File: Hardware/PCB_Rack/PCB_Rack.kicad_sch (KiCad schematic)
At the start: 31 parts, among them J1 Conn_01x03, SW1 SW_MEC_5G, SW2 SW_Push, U1 PCF8575DBR

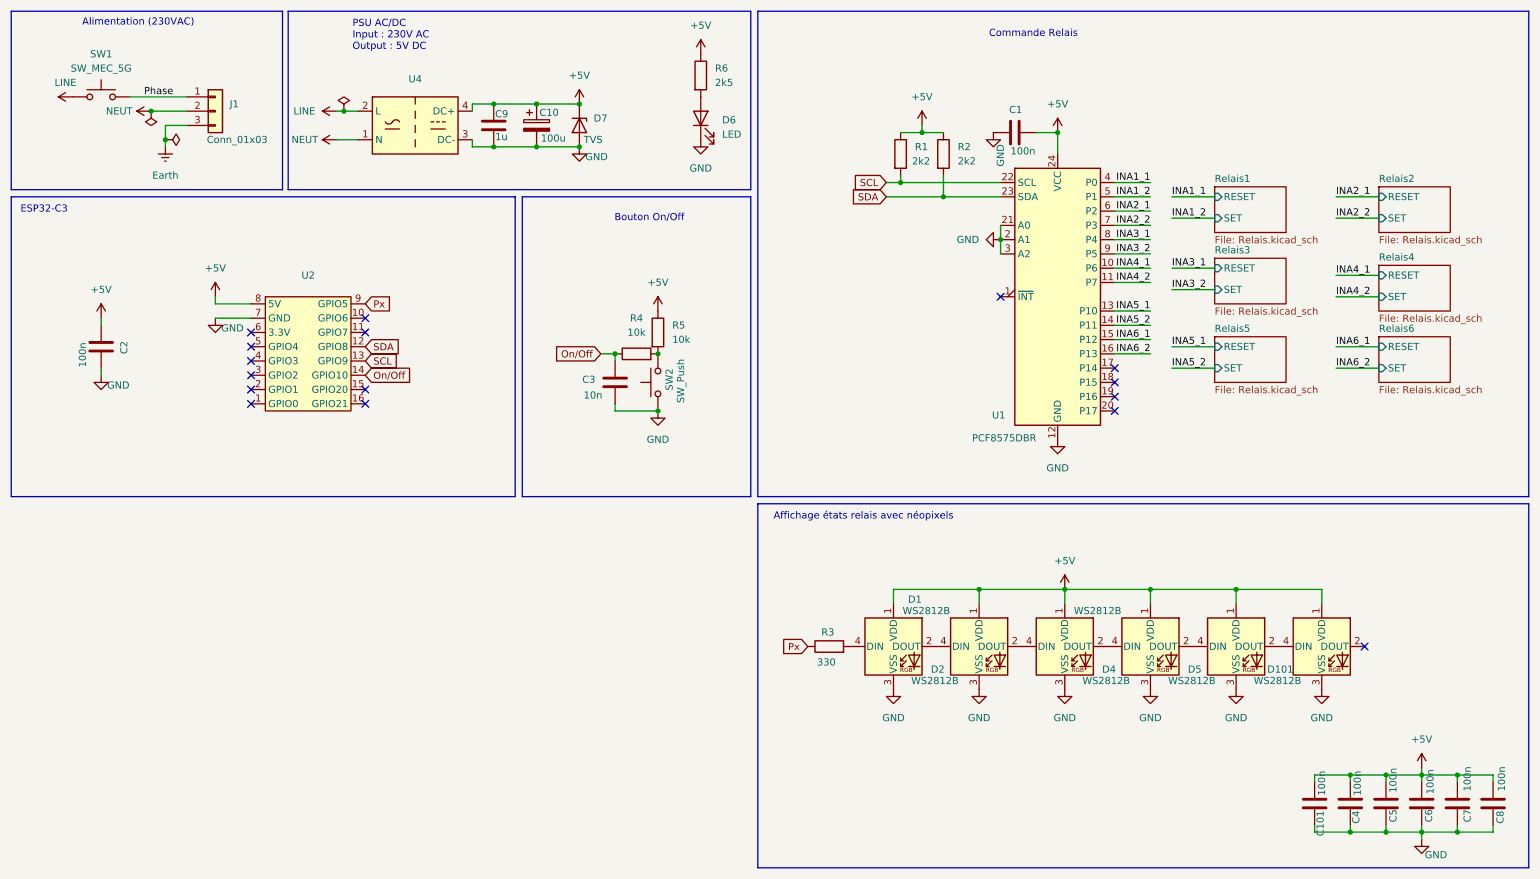
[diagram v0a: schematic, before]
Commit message: finalisation 2.0 schematic PCB RACK et début PCB
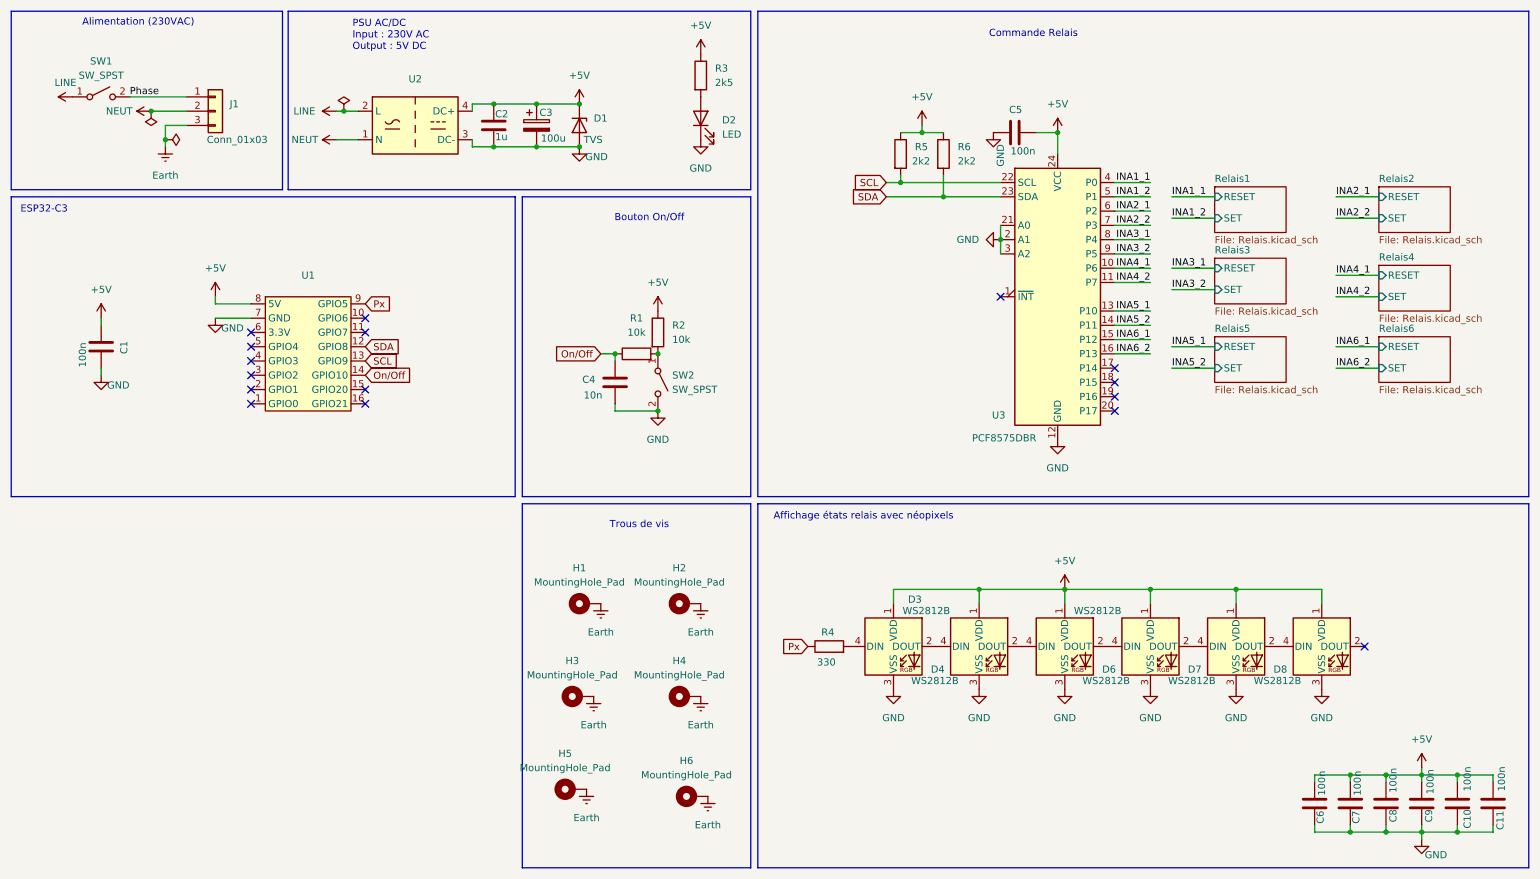
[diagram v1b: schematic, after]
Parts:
- removed SW1: SW_MEC_5G, Switch:Wurth_2pin_P5.0mm, symbol Switch:SW_MEC_5G
- removed SW2: SW_Push, Switch:Wurth_2pin_P5.0mm, symbol Switch:SW_Push
- added H1, H2, H3, H4, H5, H6: MountingHole_Pad, MountingHole:MountingHole_3.2mm_M3_DIN965_Pad_TopBottom, symbol Mechanical:MountingHole_Pad
- added SW1, SW2: SW_SPST, Switch:Wurth_2pin_P5.0mm, symbol Switch:SW_SPST
- renumbered C2 to C1, C7 to C10, C8 to C11, C9 to C2, C10 to C3, C3 to C4, C1 to C5, C101 to C6, C4 to C7, C5 to C8, C6 to C9, D7 to D1, D6 to D2, D1 to D3, D2 to D4, D3 to D5, D4 to D6, D5 to D7, D101 to D8, R4 to R1, R5 to R2, R6 to R3, R3 to R4, R1 to R5, R2 to R6, U2 to U1, U4 to U2, U1 to U3
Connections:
- net Earth: now also H1.1, H2.1, H3.1, H4.1, H5.1, H6.1
- net GND: now also SW2.2 (B)
- net LINE: now also SW1.1 (A)
- net Phase: now also SW1.2 (B)
- net at R1.2, R2.2: now also SW2.1 (A)
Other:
- note added: "Trous de vis"

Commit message: finalisation PCB Rack
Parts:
- added C12: 4u7, Capacitor_SMD:C_0603_1608Metric_Pad1.08x0.95mm_HandSolder, symbol Device:C
- added H7: MountingHole_Pad, MountingHole:MountingHole_2.2mm_M2_DIN965_Pad_TopBottom, symbol Mechanical:MountingHole_Pad
- H3, H4: footprint MountingHole:MountingHole_3.2mm_M3_DIN965_Pad_TopBottom -> MountingHole:MountingHole_2.2mm_M2_DIN965_Pad_TopBottom
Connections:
- net +5V: now also C12.1
- net Earth: now also H7.1
- net GND: now also C12.2
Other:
- moved on the sheet: H1, H2, H3, H4, H5, H6

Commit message: finalisation PCB routagev2
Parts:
- U1: footprint ESP32_C3_SuperMini:C3_SuperMini -> ESP32_C3_SuperMini:SuperMini SMT
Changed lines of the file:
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@@
 			)
 		)
-		(property "Footprint" "ESP32_C3_SuperMini:C3_SuperMini"
+		(property "Footprint" "ESP32_C3_SuperMini:SuperMini SMT"
 			(at 66.04 73.66 0)
 			(effects
